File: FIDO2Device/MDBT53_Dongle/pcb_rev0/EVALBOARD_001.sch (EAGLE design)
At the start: 1 part, among them U1 MDBT53

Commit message: 回路図を作成
・モジュール部／LED部／時刻同期部を先に掲載
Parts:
- added C1, C2: 12pF, Parts:CAP_0603
- added C8: 0.1uF, Parts:CAP_0402K
- added CN1: IF_6PIN, Connectors:IF_6PIN
- added LED1: APTD1608LSECK/J4-PF, Parts:APTD1608LSECK/J4-PF
- added LED2: APHD1608LSURCK, Parts:APHD1608LSURCK
- added LED3: APTD1608LZGCK, Parts:APTD1608LZGCK
- added LED4: APTD1608LVBC/D, Parts:APTD1608LVBC/D
- added R2, R3: 1.2k, Parts:RESISTOR_0402
- added R4: 1.8k, Parts:RESISTOR_0402
- added R5: 390, Parts:RESISTOR_0402
- added R6, R7, R8, R9: 10k, Parts:RESISTOR_0402
- added SW1: SKRPACE010, Parts:SKRPACE010
- added SW2: SKTADAE010, Parts:SKTADAE010
- added U3: RV-3028-C7, ICs:RV-3028-C7
- added X1: NX3215SA-32.768K-STD-MUA-9, Parts:NX3215SA-32.768K-STD-MUA-9
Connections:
- new net 0V: C1.2, C2.2, C8.2, CN1.1, R8.1, R9.1, SW1.S, SW1.S1, SW2.S, SW2.S1, U1.GND@1, U1.GND@24, U1.GND@42, U1.GND@61, U3.VSS
- new net DCC: U1.DCC
- new net DCCD: U1.DCCD
- new net DCCH: U1.DCCH
- new net DECD: U1.DECD
- new net DECR: U1.DECR
- new net D_N: U1.D-
- new net D_P: U1.D+
- new net LED1: R2.1, U1.P0.28/AIN7
- new net LED2: R3.1, U1.P0.29
- new net LED3: R4.1, U1.P0.30
- new net LED4: R5.1, U1.P0.31
- new net N$1: LED4.C, R5.2
- new net N$10: R8.2, U3.EVI
- new net N$6: LED3.C, R4.2
- new net N$7: LED2.C, R3.2
- new net N$8: LED1.C, R2.2
- new net N$9: R9.2, U3.VBACKUP
- new net RESET: CN1.5, SW2.P, SW2.P1, U1.RESET
- new net SCL: R7.1, U1.P1.03/TWI, U3.SCL@
- new net SDA: R6.1, U1.P1.02/TWI, U3.SDA@
- new net SW1: SW1.P, SW1.P1, U1.P0.23
- new net SWDCLK: CN1.4, U1.SWDCLK
- new net SWDIO: CN1.3, U1.SWDIO
- new net TXD: CN1.6, U1.P0.20
- new net VBUS_NRF: U1.VBUS
- new net VDDH: U1.VDDH
- new net VDD_NRF: C8.1, CN1.2, LED1.A, LED2.A, LED3.A, LED4.A, R6.2, R7.2, U1.VDD, U3.VDD
- new net XL1: C1.1, U1.P0.00/XL1, X1.1
- new net XL2: C2.1, U1.P0.01/XL2, X1.2
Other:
- note added: "32.768kHzクリスタル"
- note added: "Eval board for MDBT53 Dongle"
- note added: "LED部"
- note added: "LED（緑色）"
- note added: "LED（赤色）"
- note added: "LED（青色）"
- note added: "LED（黄色）"
- note added: "MAIN SW"
- note added: "nRF5340アプリケーションを 書込する際に使用します。"
- note added: "プログラミングI/F部"
- note added: "ボタン乾電池を装着すると、常時給電されます。"
- note added: "モジュール部"
- note added: "リセット回路"
- note added: "時刻同期部"
- note removed: "MDBT53 Dongle evaluation board"

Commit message: 回路図を作成
・USBコネクター部を追加掲載
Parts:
- removed C8: 0.1uF, Parts:CAP_0402K
- added C3: 0.01uF, Parts:CAP_0402K
- added C4, C5, C7: 0.1uF, Parts:CAP_0402K
- added C6: 10uF, Parts:CAP_0603
- added CN2: USB4105-GF-A, Connectors:USB4105-GF-A
- added D1: PRTR5V0U2X, Parts:PRTR5V0U2X
- added L1, L2, L3, L4: BLM15AG121SN1D, Parts:BLM15AG121SN1D
- added R1: 5.1k, Parts:RESISTOR_0402
- added R10: 10k, Parts:RESISTOR_0402
- R2: value 1.2k -> 5.1k
- R4: value 1.8k -> 1.2k
- R5: value 390 -> 1.8k
- R6: value 10k -> 390
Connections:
- new net FG: CN2.FG1, CN2.FG2, CN2.FG3, CN2.FG4, L4.1
- new net N$2: CN2.CC1, R1.2
- new net N$3: CN2.CC2, R2.2
- new net USB_GND: CN2.GND1, CN2.GND2, L3.1, R1.1, R2.1
- new net VBATT: C7.1, U3.VDD
- new net VBUS: C3.1, C5.1, C6.1, CN2.VBUS1, CN2.VBUS2, D1.VCC, L1.1, L2.1
- new net VBUS_CONN: C4.1, L2.2
- new net VBUS_LDO: L1.2
- net 0V: now also C3.2, C4.2, C5.2, C6.2, C7.2, D1.GND, L3.2, L4.2, R10.1; no longer C8.2, R8.1
- net D_N: now also CN2.D_N1, CN2.D_N2, D1.I/O_1
- net D_P: now also CN2.D_P1, CN2.D_P2, D1.I/O_2
- net LED1: now also R3.1; no longer R2.1
- net LED2: now also R4.1; no longer R3.1
- net LED3: now also R5.1; no longer R4.1
- net LED4: now also R6.1; no longer R5.1
- net N$1: now also R6.2; no longer R5.2
- net N$10: now also R9.2; no longer R8.2
- net N$6: now also R5.2; no longer R4.2
- net N$7: now also R4.2; no longer R3.2
- net N$8: now also R3.2; no longer R2.2
- net N$9: now also R10.2; no longer R9.2
- net SCL: now also R8.1; no longer R7.1
- net SDA: now also R7.1; no longer R6.1
- net VDD_NRF: now also R8.2; no longer C8.1, R6.2, U3.VDD
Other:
- note added: "USB-Cメス コネクターを 実装"
- note added: "USBコネクター部"

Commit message: 回路図を作成
・電源供給部を追加掲載
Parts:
- added BAT1: BAT-HLD-012-SMT, Connectors:BAT-HLD-012-SMT
- added BAT2: 1072TR, Connectors:1072TR
- added C8, C9: 1uF, Parts:CAP_0603
- added D2, D3, D4: PMEG2005AEA,115, Parts:PMEG2005AEA,115
- added U2: XC6206P332MR-G, Parts:XC6206P332MR-G
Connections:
- new net VBAT_1225: BAT1.+, D3.A
- new net VBAT_2032: BAT2.+, D4.A
- new net VDD_3V3: C9.1, D2.A, U2.VOUT
- net 0V: now also BAT1.-, BAT2.-, C8.2, C9.2, U2.VSS
- net VBUS_LDO: now also C8.1, U2.VIN
- net VDD_NRF: now also D2.C, D3.C, D4.C
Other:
- note added: "USBポートに装着時は、VBUSの5.0V-->3.3Vに降圧して供給します。 乾電池ホルダーにボタン乾電池を装着した場合は、3.0Vを供給します。"
- note added: "ボタン乾電池ケース（1225）"
- note added: "ボタン乾電池ケース（2032）"
- note added: "逆流回避用"
- note added: "電源供給部"
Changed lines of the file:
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@@
 <part name="GND15" library="Supply" deviceset="0V" device=""/>
 <part name="CN1" library="Connectors" deviceset="IF_6PIN" device=""/>
+<part name="FRAME4" library="Generic" deviceset="A4L-LOC" device=""/>
+<part name="C8" library="Parts" deviceset="CAP" device="_0603" value="1uF"/>
+<part name="C9" library="Parts" deviceset="CAP" device="_0603" value="1uF"/>
+<part name="GND16" library="Supply" deviceset="0V" device=""/>
+<part name="GND17" library="Supply" deviceset="0V" device=""/>
+<part name="GND18" library="Supply" deviceset="0V" device=""/>
+<part name="BAT1" library="Connectors" deviceset="BAT-HLD-012-SMT" device=""/>
+<part name="GND19" library="Supply" deviceset="0V" device=""/>
+<part name="U2" library="Parts" deviceset="XC6206" device="P332MR-G"/>
+<part name="GND6" library="Supply" deviceset="0V" device=""/>
+<part name="D2" library="Parts" deviceset="PMEG2005" device="AEA,115"/>
+<part name="D3" library="Parts" deviceset="PMEG2005" device="AEA,115"/>
+<part name="D4" library="Parts" deviceset="PMEG2005" device="AEA,115"/>
+<part name="BAT2" library="Connectors" deviceset="1072" device="TR"/>
 </parts>
 <sheets>
@@
 </segment>
 </net>
+</nets>
+</sheet>
+<sheet>
+<plain>
+<text x="217.424" y="20.32" size="1.778" layer="91">Eval board for MDBT53 Dongle</text>
+<text x="168.91" y="8.89" size="3.81" layer="91">MDBT53 Dongle
+    （rev0）</text>
+<text x="48.26" y="144.78" size="3.81" layer="91">電源供給部</text>
+<text x="48.26" y="139.7" size="2.54" layer="91" align="top-left">USBポートに装着時は、VBUSの5.0V--&gt;3.3Vに降圧して供給します。
+乾電池ホルダーにボタン乾電池を装着した場合は、3.0Vを供給します。</text>
+<text x="48.26" y="88.9" size="2.54" layer="91" align="top-left">ボタン乾電池ケース（1225）</text>
+<text x="170.18" y="109.22" size="2.54" layer="91" align="top-left">逆流回避用</text>
+<text x="48.26" y="55.88" size="2.54" layer="91" align="top-left">ボタン乾電池ケース（2032）</text>
+</plain>
+<instances>
+<instance part="FRAME4" gate="G$1" x="0" y="0"/>
+<instance part="C8" gate="G$1" x="76.2" y="114.3"/>
+<instance part="C9" gate="G$1" x="119.38" y="114.3"/>
+<instance part="GND16" gate="1" x="76.2" y="99.06"/>
+<instance part="GND17" gate="1" x="111.76" y="99.06"/>
+<instance part="GND18" gate="1" x="119.38" y="99.06"/>
+<instance part="BAT1" gate="G$1" x="76.2" y="78.74"/>
+<instance part="GND19" gate="1" x="50.8" y="68.58"/>
+<instance part="U2" gate="G$1" x="83.82" y="121.92"/>
+<instance part="GND6" gate="1" x="50.8" y="35.56"/>
+<instance part="D2" gate="G$1" x="177.8" y="91.44"/>
+<instance part="D3" gate="G$1" x="177.8" y="81.28"/>
+<instance part="D4" gate="G$1" x="177.8" y="71.12"/>
+<instance part="BAT2" gate="G$1" x="76.2" y="45.72"/>
+</instances>
+<busses>
+</busses>
+<nets>
+<net name="0V" class="0">
+<segment>
+<pinref part="BAT1" gate="G$1" pin="-"/>
+<pinref part="GND19" gate="1" pin="0V"/>
+<wire x1="71.12" y1="78.74" x2="50.8" y2="78.74" width="0.1524" layer="91"/>
+<wire x1="50.8" y1="78.74" x2="50.8" y2="71.12" width="0.1524" layer="91"/>
+</segment>
+<segment>
+<pinref part="U2" gate="G$1" pin="VSS"/>
+<pinref part="GND17" gate="1" pin="0V"/>
+<wire x1="106.68" y1="116.84" x2="111.76" y2="116.84" width="0.1524" layer="91"/>
+<wire x1="111.76" y1="116.84" x2="111.76" y2="101.6" width="0.1524" layer="91"/>
+</segment>
+<segment>
+<pinref part="C8" gate="G$1" pin="2"/>
+<pinref part="GND16" gate="1" pin="0V"/>
+<wire x1="76.2" y1="106.68" x2="76.2" y2="101.6" width="0.1524" layer="91"/>
+</segment>
+<segment>
+<pinref part="C9" gate="G$1" pin="2"/>
+<pinref part="GND18" gate="1" pin="0V"/>
+<wire x1="119.38" y1="106.68" x2="119.38" y2="101.6" width="0.1524" layer="91"/>
+</segment>
+<segment>
+<pinref part="GND6" gate="1" pin="0V"/>
+<wire x1="50.8" y1="38.1" x2="50.8" y2="45.72" width="0.1524" layer="91"/>
+<wire x1="50.8" y1="45.72" x2="71.12" y2="45.72" width="0.1524" layer="91"/>
+<pinref part="BAT2" gate="G$1" pin="-"/>
+</segment>
+</net>
+<net name="VDD_3V3" class="0">
+<segment>
+<pinref part="U2" gate="G$1" pin="VOUT"/>
+<pinref part="C9" gate="G$1" pin="1"/>
+<wire x1="106.68" y1="121.92" x2="119.38" y2="121.92" width="0.1524" layer="91"/>
+<wire x1="119.38" y1="121.92" x2="119.38" y2="114.3" width="0.1524" layer="91"/>
+<wire x1="119.38" y1="121.92" x2="129.54" y2="121.92" width="0.1524" layer="91"/>
+<junction x="119.38" y="121.92"/>
+<label x="129.54" y="121.92" size="1.778" layer="95" xref="yes"/>
+</segment>
+<segment>
+<wire x1="167.64" y1="91.44" x2="175.26" y2="91.44" width="0.1524" layer="91"/>
+<pinref part="D2" gate="G$1" pin="A"/>
+<label x="167.64" y="91.44" size="1.778" layer="95" rot="R180" xref="yes"/>
+</segment>
+</net>
+<net name="VBUS_LDO" class="0">
+<segment>
+<pinref part="U2" gate="G$1" pin="VIN"/>
+<wire x1="83.82" y1="119.38" x2="76.2" y2="119.38" width="0.1524" layer="91"/>
+<pinref part="C8" gate="G$1" pin="1"/>
+<wire x1="76.2" y1="119.38" x2="68.58" y2="119.38" width="0.1524" layer="91"/>
+<wire x1="76.2" y1="114.3" x2="76.2" y2="119.38" width="0.1524" layer="91"/>
+<junction x="76.2" y="119.38"/>
+<label x="68.58" y="119.38" size="1.778" layer="95" rot="R180" xref="yes"/>
+</segment>
+</net>
+<net name="VBAT_1225" class="0">
+<segment>
+<pinref part="BAT1" gate="G$1" pin="+"/>
+<wire x1="81.28" y1="78.74" x2="101.6" y2="78.74" width="0.1524" layer="91"/>
+<label x="101.6" y="78.74" size="1.778" layer="95" xref="yes"/>
+</segment>
+<segment>
+<pinref part="D3" gate="G$1" pin="A"/>
+<wire x1="175.26" y1="81.28" x2="167.64" y2="81.28" width="0.1524" layer="91"/>
+<label x="167.64" y="81.28" size="1.778" layer="95" rot="R180" xref="yes"/>
+</segment>
+</net>
+<net name="VBAT_2032" class="0">
+<segment>
+<wire x1="81.28" y1="45.72" x2="101.6" y2="45.72" width="0.1524" layer="91"/>
+<label x="101.6" y="45.72" size="1.778" layer="95" xref="yes"/>
+<pinref part="BAT2" gate="G$1" pin="+"/>
+</segment>
+<segment>
+<pinref part="D4" gate="G$1" pin="A"/>
+<wire x1="175.26" y1="71.12" x2="167.64" y2="71.12" width="0.1524" layer="91"/>
+<label x="167.64" y="71.12" size="1.778" layer="95" rot="R180" xref="yes"/>
+</segment>
+</net>
+<net name="VDD_NRF" class="0">
+<segment>
+<pinref part="D3" gate="G$1" pin="C"/>
+<wire x1="180.34" y1="81.28" x2="205.74" y2="81.28" width="0.1524" layer="91"/>
+<label x="213.36" y="81.28" size="1.778" layer="95" xref="yes"/>
+<pinref part="D2" gate="G$1" pin="C"/>
+<wire x1="205.74" y1="81.28" x2="213.36" y2="81.28" width="0.1524" layer="91"/>
+<wire x1="180.34" y1="91.44" x2="205.74" y2="91.44" width="0.1524" layer="91"/>
+<wire x1="205.74" y1="91.44" x2="205.74" y2="81.28" width="0.1524" layer="91"/>
+<pinref part="D4" gate="G$1" pin="C"/>
+<wire x1="205.74" y1="81.28" x2="205.74" y2="71.12" width="0.1524" layer="91"/>
+<wire x1="205.74" y1="71.12" x2="180.34" y2="71.12" width="0.1524" layer="91"/>
+<junction x="205.74" y="81.28"/>
+</segment>
+</net>

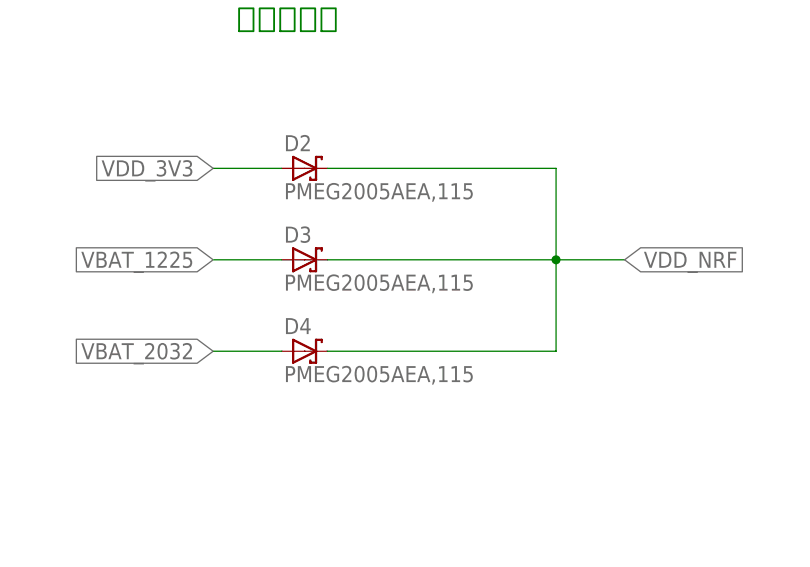
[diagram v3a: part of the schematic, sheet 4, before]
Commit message: 回路図を作成
・逆流阻止SBDを小型の部品と差し替え
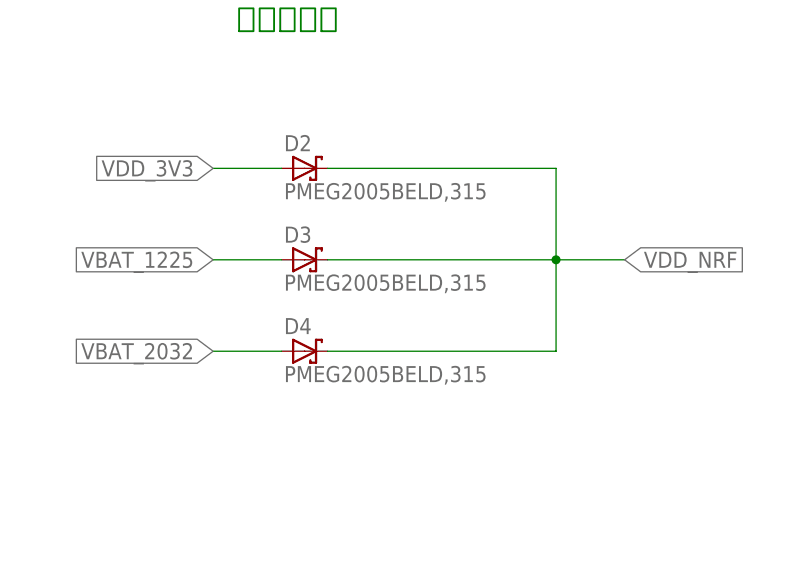
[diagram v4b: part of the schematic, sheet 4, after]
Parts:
- D2, D3, D4: value PMEG2005AEA,115 -> PMEG2005BELD,315; device Parts:PMEG2005AEA,115 -> Parts:PMEG2005BELD,315
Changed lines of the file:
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@@
 <part name="U2" library="Parts" deviceset="XC6206" device="P332MR-G"/>
 <part name="GND6" library="Supply" deviceset="0V" device=""/>
-<part name="D2" library="Parts" deviceset="PMEG2005" device="AEA,115"/>
-<part name="D3" library="Parts" deviceset="PMEG2005" device="AEA,115"/>
-<part name="D4" library="Parts" deviceset="PMEG2005" device="AEA,115"/>
+<part name="D2" library="Parts" deviceset="PMEG2005" device="BELD,315" value="PMEG2005BELD,315"/>
+<part name="D3" library="Parts" deviceset="PMEG2005" device="BELD,315" value="PMEG2005BELD,315"/>
+<part name="D4" library="Parts" deviceset="PMEG2005" device="BELD,315" value="PMEG2005BELD,315"/>
 <part name="BAT2" library="Connectors" deviceset="1072" device="TR"/>
 </parts>

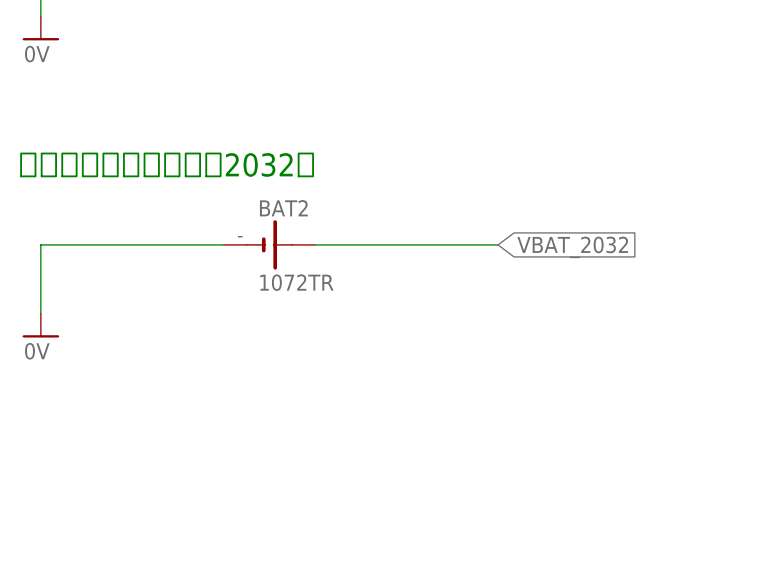
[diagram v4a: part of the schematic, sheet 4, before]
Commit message: 回路図を作成
・電池ケースを１点追加
（為念でCR2032を評価するための措置）
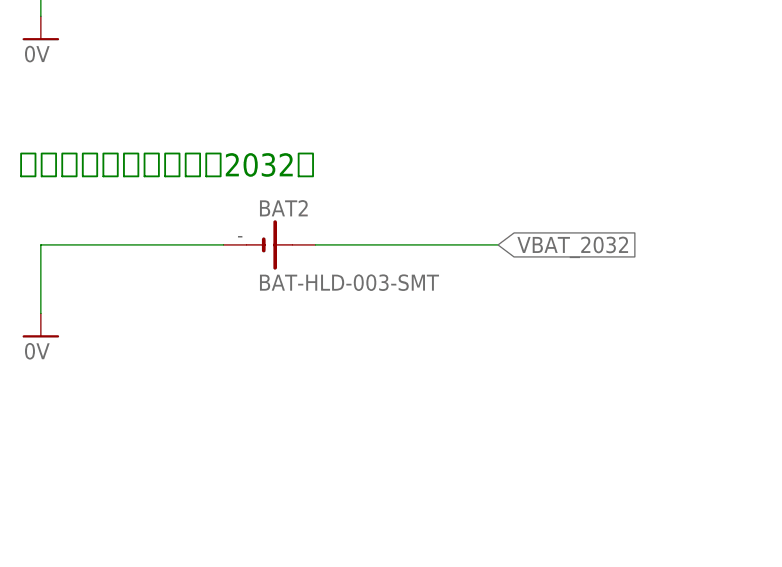
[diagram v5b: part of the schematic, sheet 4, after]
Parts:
- BAT2: value 1072TR -> BAT-HLD-003-SMT; device Connectors:1072TR -> Connectors:BAT-HLD-003-SMT
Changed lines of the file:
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@@
 <part name="D3" library="Parts" deviceset="PMEG2005" device="BELD,315" value="PMEG2005BELD,315"/>
 <part name="D4" library="Parts" deviceset="PMEG2005" device="BELD,315" value="PMEG2005BELD,315"/>
-<part name="BAT2" library="Connectors" deviceset="1072" device="TR"/>
+<part name="BAT2" library="Connectors" deviceset="BAT-HLD-003-SMT" device=""/>
 </parts>
 <sheets>
